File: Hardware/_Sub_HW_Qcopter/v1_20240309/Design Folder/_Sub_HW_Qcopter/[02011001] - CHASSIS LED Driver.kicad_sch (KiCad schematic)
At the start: 2 parts, among them J1601 HDR_1X2_VERT

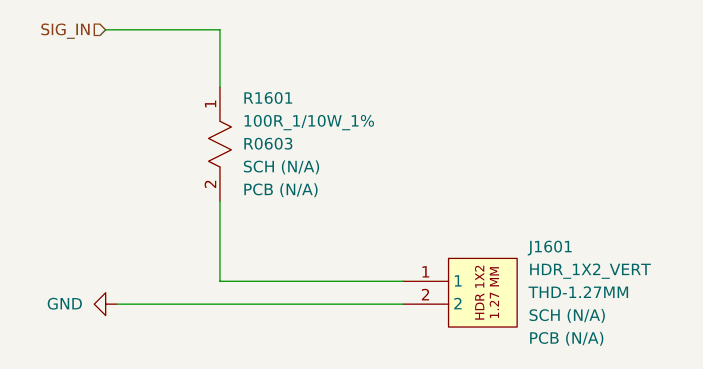
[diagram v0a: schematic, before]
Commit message: Update [02011001] - CHASSIS LED Driver.kicad_sch
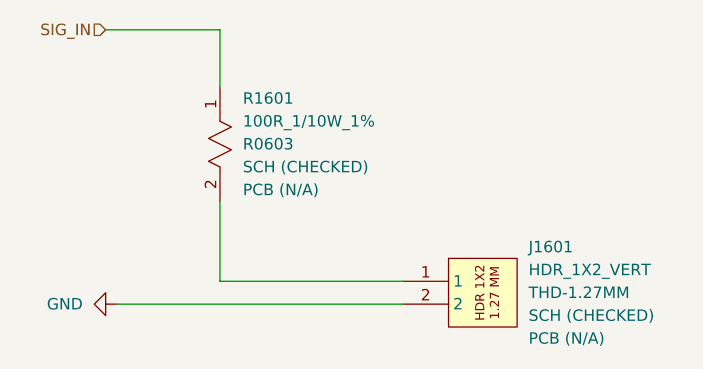
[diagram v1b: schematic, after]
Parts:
- J1601, R1601: SCH CHECK SCH (N/A) -> SCH (CHECKED)
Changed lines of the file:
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@@
 			)
 		)
-		(property "SCH CHECK" "SCH (N/A)"
+		(property "SCH CHECK" "SCH (CHECKED)"
 			(at 288.29 209.5499 0)
 			(effects
@@
 			)
 		)
-		(property "SCH CHECK" "SCH (N/A)"
+		(property "SCH CHECK" "SCH (CHECKED)"
 			(at 256.54 193.0399 90)
 			(effects
